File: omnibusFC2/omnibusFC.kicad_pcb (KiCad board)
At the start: 4 copper layers, 36 x 36 mm, 116 parts, among them J1 Conn_03, J10 Conn_06, J11 Conn_06, J12 Conn03, J13 Conn03, J15 Conn03, J16 Conn_01x01, J17 Conn_01x01, J2 Con02, J3 Conn_01x01, J4 Conn_06, J5 Conn_04, J6 Con02, J7 Conn03, J8 Conn_03, J9 Con02, Q1 MMBT3904, Q2 MMBT3904, Q3 MMBT3904, SW1 SW_Push, U1 STM32F405RGT6, U10 Micro_SD_Card_Det, U11 INA139, U2 MP1593, U3 MPU-9250, U4 MIC5332-SSYMT-TR, U9 MS5611-01BA, Y1 Crystal

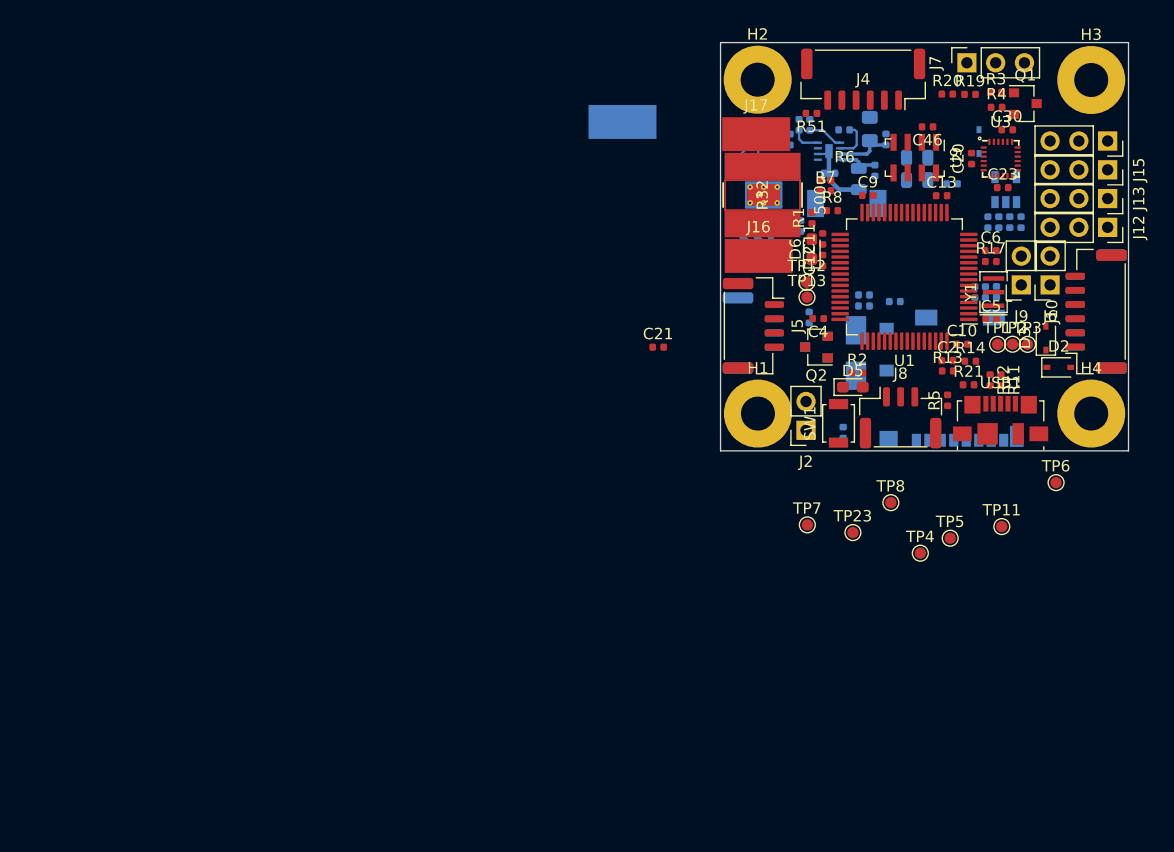
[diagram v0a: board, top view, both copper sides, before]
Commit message: 보드크기변경
그리기 어려워서 Multiwii_lite크기로 변경
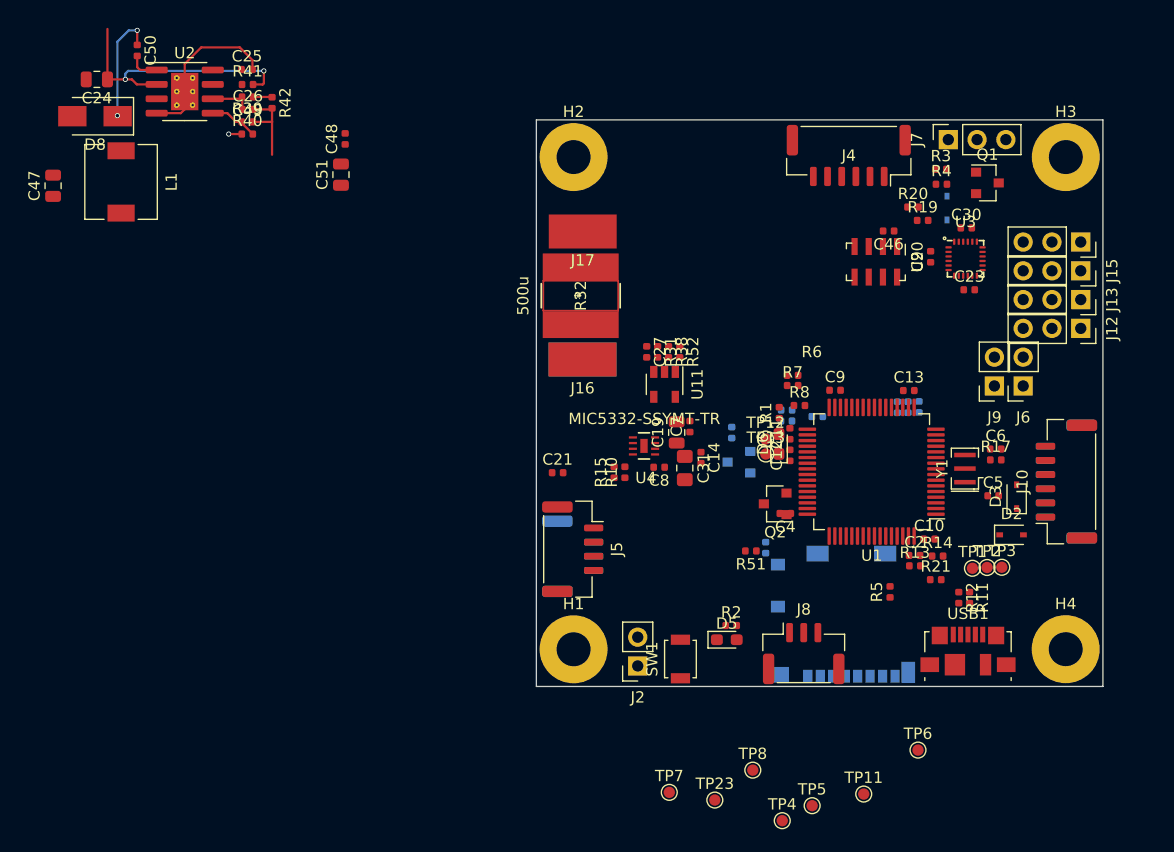
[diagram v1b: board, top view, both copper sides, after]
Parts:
- C14, C19, C24, C25, C26, C27, C31, C47, C48, C49, C50, C51, C7, C8, D8, L1, R10, R15, R31, R38, R39, R40, R41, R42, R52, U11, U2, U4: moved to F.Cu
- J16: value Conn_01x01 -> BAT
- J17: value Conn_01x01 -> MOT
- J3: value Conn_01x01 -> GND
- moved C47 76.3 mm to (68.3, 77.9), turned to 90 degrees
- moved D8 70.3 mm to (72.0, 71.7), turned to 180 degrees
- moved L1 64.1 mm to (74.3, 77.5), turned to 270 degrees
- moved C24 60.6 mm to (72.2, 68.5)
- moved C50 60.6 mm to (75.8, 65.9), turned to 270 degrees
- moved C48 53.7 mm to (94.1, 73.7), turned to 90 degrees
- moved C25 52.2 mm to (85.4, 67.6)
- moved U2 51.9 mm to (79.9, 69.5), turned to 0 degrees
- moved C51 50.9 mm to (93.7, 76.9), turned to 90 degrees
- moved R41 48.1 mm to (85.5, 68.9), turned to 0 degrees
- moved C49 46.2 mm to (85.5, 70.0), turned to 180 degrees
- moved C26 45.1 mm to (85.5, 71.1), turned to 0 degrees
- moved R42 44.9 mm to (87.7, 70.5), turned to 270 degrees
- moved R40 44.1 mm to (85.5, 73.3), turned to 0 degrees
- moved R39 43.2 mm to (85.5, 72.2), turned to 0 degrees
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- renumbered dddddddddd to J14
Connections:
- J17 pad 1: GND -> Net-(C24-Pad1)
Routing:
- net Net-(C24-Pad1): track 2.95 -> 23.9 mm, vias 0 -> 2
- net GND: track 9.82 -> 22.0 mm
- net /VCC3v3: track 5.24 -> 0.00 mm
- net Net-(C50-Pad1): track 5.19 -> 9.97 mm, vias 0 -> 2
- net /VCC_RC: track 3.84 -> 0.00 mm
- net Net-(C8-Pad1): track 3.47 -> 0.00 mm
- net Net-(R10-Pad2): track 3.12 -> 0.00 mm
- net Net-(C50-Pad2): track 0.00 -> 2.81 mm
- net Net-(R15-Pad2): track 2.57 -> 0.00 mm
- net Net-(R39-Pad1): track 3.07 -> 4.36 mm
- net /VCC5_DC: track 0.00 -> 1.16 mm, vias 0 -> 1
- net Net-(C49-Pad1): track 0.94 -> 1.69 mm
- net /SPI3_MISO: track 0.74 -> 0.00 mm
- net Net-(U1-Pad5): track 0.60 -> 0.00 mm
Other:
- board size 36 x 36 mm -> 50 x 50 mm
